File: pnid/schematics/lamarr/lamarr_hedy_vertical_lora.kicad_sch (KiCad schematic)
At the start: 59 parts, among them U1 Rocket_Big

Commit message: various fixes
configure lora use,
fix guidance & navigation pnid,
fix retract threshold
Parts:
- removed ClearFlash: Flash:Clear, symbol PnID-Lib:Label
- removed Logging: Logging, symbol PnID-Lib:Label
- added ClearFlash1: Flash:Clear, symbol PnID-Lib:Label
- added Engine: lora:engine_ecu:LoggingEnabled, symbol PnID-Lib:LED
- added Engine: lora:ecu:FlashStatus, symbol PnID-Lib:LED
- added Fuel: lora:fuel_ecu:LoggingEnabled, symbol PnID-Lib:LED
- added Fuel: lora:fuel_ecu:FlashStatus, symbol PnID-Lib:LED
- added Logging1: Logging, symbol PnID-Lib:Label
- added Ox: lora:ox_ecu:FlashStatus, symbol PnID-Lib:LED
- added Ox: lora:ox_ecu:LoggingEnabled, symbol PnID-Lib:LED
- added RCU: lora:rcu:FlashStatus, symbol PnID-Lib:LED
- added RCU: lora:rcu:LoggingEnabled, symbol PnID-Lib:LED
- Voltages: value RocketVoltages -> RocketVoltagesLora
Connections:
- net at engine.~ (O): now also venturi1.~
- net at ox_venturi.~: now also ox_main_valve.~, ox_venturi_pressure.~; no longer engine.~ (O)
- net at venturi1.~: now also fuel_main_valve.~, fuel_venturi_pressure.~; no longer engine.~ (O)
- new net: engine.~ (O), ox_venturi.~
- new net: OX.~, ox_main_valve.~, ox_quick_connect.~
- new net: Orifice1.~, ox_pressurant_valve.~, pressurantPressureRegulator2.~
- new net: FUEL.~, fuel_main_valve.~, ox_quick_connect1.~
- new net: Orifice2.~, fuel_pressurant_valve.~, pressurantPressureRegulator1.~

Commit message: i mog schlafn
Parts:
- Engine: value lora:ecu:FlashStatus -> lora:engine_ecu:FlashStatus
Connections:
- net at engine.~ (O): now also venturi1.~
- net at ox_venturi.~: now also ox_main_valve.~, ox_venturi_pressure.~; no longer engine.~ (O)
- net at venturi1.~: now also fuel_main_valve.~, fuel_venturi_pressure.~; no longer engine.~ (O)
- new net: engine.~ (O), ox_venturi.~
- new net: OX.~, ox_main_valve.~, ox_quick_connect.~
- new net: Orifice1.~, ox_pressurant_valve.~, pressurantPressureRegulator2.~
- new net: FUEL.~, fuel_main_valve.~, ox_quick_connect1.~
- new net: Orifice2.~, fuel_pressurant_valve.~, pressurantPressureRegulator1.~
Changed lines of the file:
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@@
 			)
 		)
-		(property "Value" "lora:ecu:FlashStatus"
+		(property "Value" "lora:engine_ecu:FlashStatus"
 			(at 13.716 -131.318 90)
 			(effects

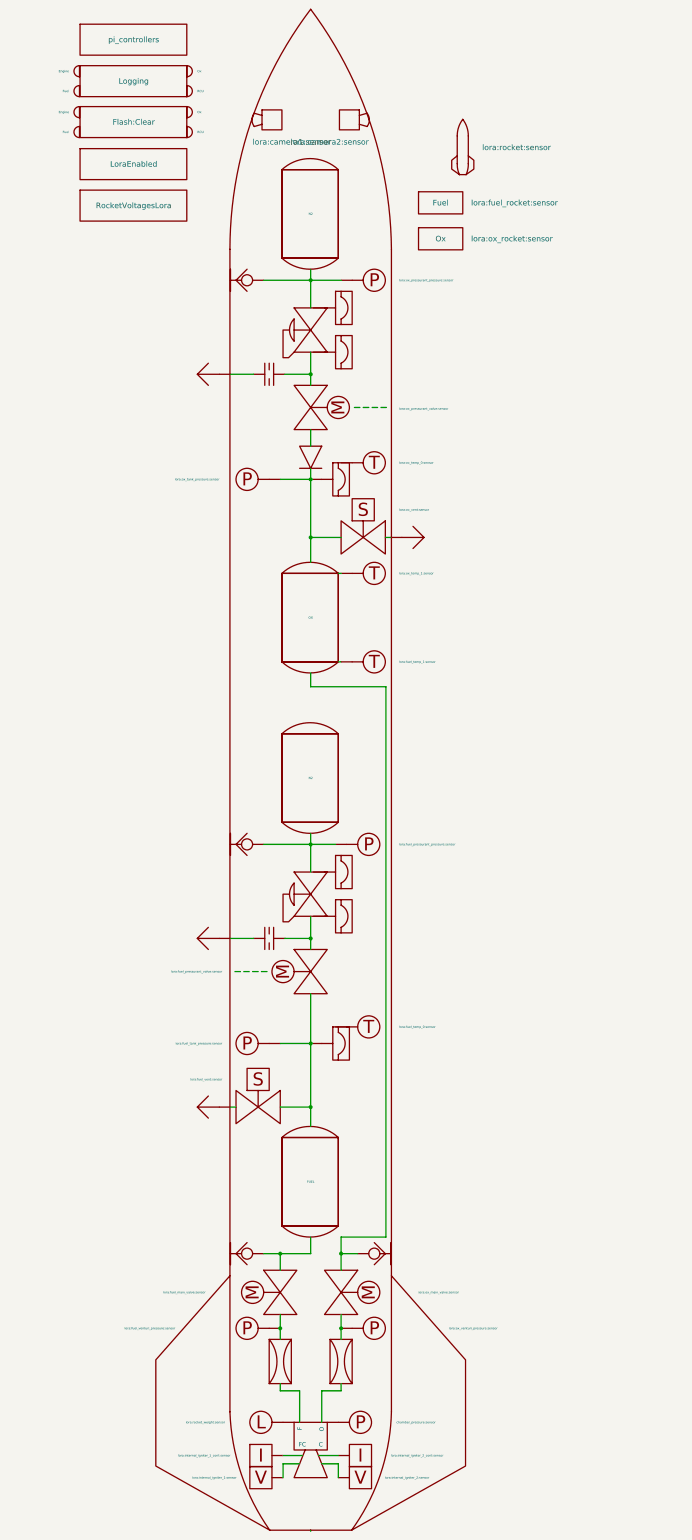
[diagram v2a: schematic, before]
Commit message: more refinements in sensor calibration & ECUI look
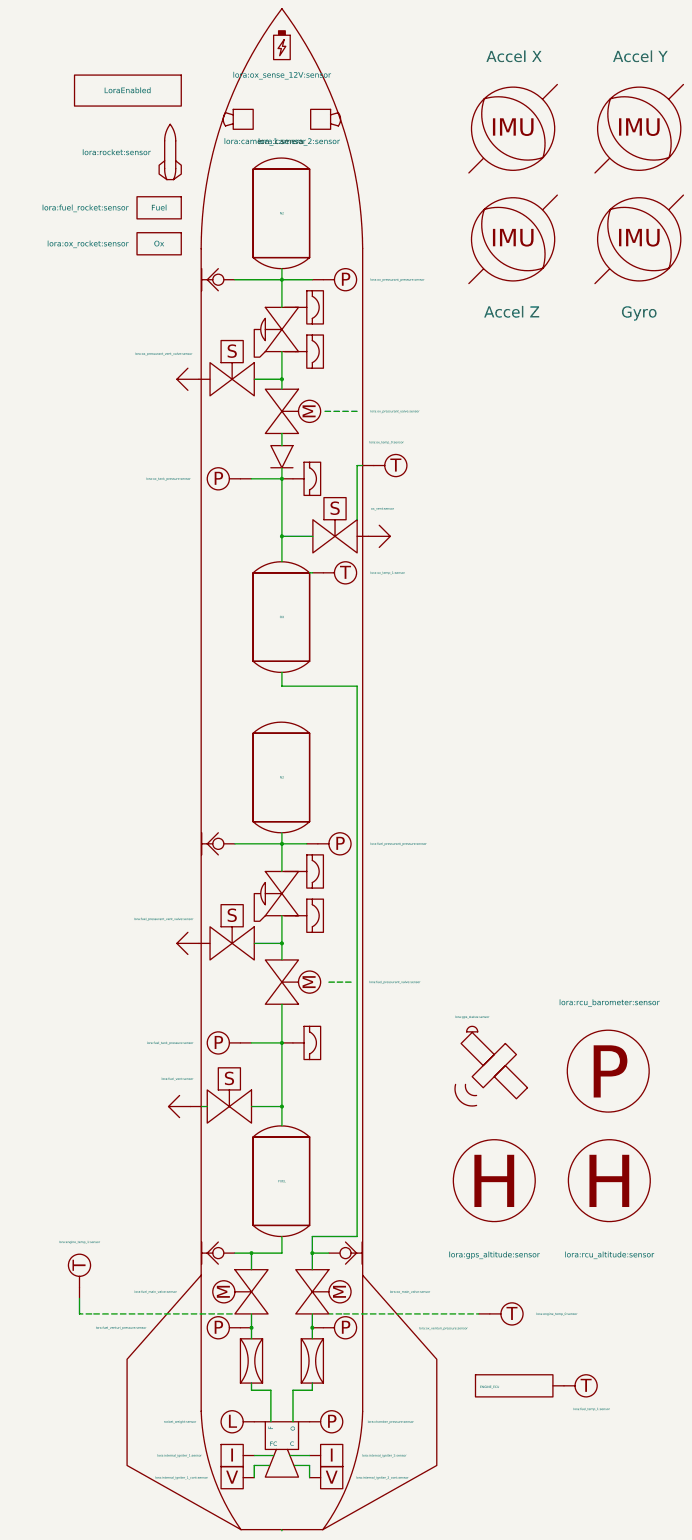
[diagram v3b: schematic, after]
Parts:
- removed ClearFlash1: Flash:Clear, symbol PnID-Lib:Label
- removed Engine: lora:engine_ecu:LoggingEnabled, symbol PnID-Lib:LED
- removed Engine: lora:engine_ecu:FlashStatus, symbol PnID-Lib:LED
- removed Fuel: lora:fuel_ecu:LoggingEnabled, symbol PnID-Lib:LED
- removed Fuel: lora:fuel_ecu:FlashStatus, symbol PnID-Lib:LED
- removed Logging1: Logging, symbol PnID-Lib:Label
- removed Orifice1, Orifice2: Orifice, symbol PnID-Lib:Orifice
- removed Ox: lora:ox_ecu:FlashStatus, symbol PnID-Lib:LED
- removed Ox: lora:ox_ecu:LoggingEnabled, symbol PnID-Lib:LED
- removed PI_Contollers: pi_controllers, symbol PnID-Lib:Label
- removed RCU: lora:rcu:FlashStatus, symbol PnID-Lib:LED
- removed RCU: lora:rcu:LoggingEnabled, symbol PnID-Lib:LED
- removed Voltages: RocketVoltagesLora, symbol PnID-Lib:Label
- removed fuel_manifold_temperature: lora:fuel_temp_0:sensor, symbol PnID-Lib:Sensor_Temperature
- removed ox_manifold_temperature: lora:ox_temp_0:sensor, symbol PnID-Lib:Sensor_Temperature
- added Accel_X: accel_x, symbol PnID-Lib:IMU
- added Accel_Y: accel_y, symbol PnID-Lib:IMU
- added Accel_Z: accel_z, symbol PnID-Lib:IMU
- added Gyro: gyro_x_y_z, symbol PnID-Lib:IMU
- added U2: lora:ox_sense_12V:sensor, symbol PnID-Lib:Battery
- added ecu_flash_status?: lora:gps_status:sensor, symbol PnID-Lib:LED
- added engine_ECU_temperature: lora:fuel_temp_1:sensor, symbol PnID-Lib:Sensor_Temperature
- added engineecu1: ENGINE_ECU, symbol PnID:Label
- added fuel_main_valve_servo_temperature: lora:engine_temp_1:sensor, symbol PnID-Lib:Sensor_Temperature
- added fuel_pressurant_vent_valve: lora:fuel_pressurant_vent_valve:sensor, symbol PnID-Lib:Valve_Solenoid_NO
- added gnss: GNSSLora, symbol PnID-Lib:GNSS
- added gps_altitude: lora:gps_altitude:sensor, symbol PnID-Lib:Sensor_Height
- added ox_pressurant_vent_valve: lora:ox_pressurant_vent_valve:sensor, symbol PnID-Lib:Valve_Solenoid_NO
- added ox_vent_temperature: lora:ox_temp_0:sensor, symbol PnID-Lib:Sensor_Temperature
- added rcu_altitude: lora:rcu_altitude:sensor, symbol PnID-Lib:Sensor_Height
- added rcu_barometer: lora:rcu_barometer:sensor, symbol PnID-Lib:Sensor_Pressure_Big
- C6: value lora:camera2:sensor -> lora:camera_2:sensor
- C7: value lora:camera1:sensor -> lora:camera_1:sensor
- chamber_pressure: value chamber_pressure:sensor -> lora:chamber_pressure:sensor
- igniter1: value lora:internal_igniter_1_cont:sensor -> lora:internal_igniter_1:sensor
- igniter2: value lora:internal_igniter_2_cont:sensor -> lora:internal_igniter_2:sensor
- ox_main_valve_servo_temperature: renamed from ox_tank_bottom_temperature; value lora:fuel_temp_1:sensor -> lora:engine_temp_0:sensor
- ox_vent: value lora:ox_vent:sensor -> ox_vent:sensor
- ox_venturi: value lora:ox_venturi:sensor -> ox_venturi:sensor
- thrust: value lora:rocket_weight:sensor -> rocket_weight:sensor
- venturi1: value lora:venturi:sensor -> venturi:sensor
- voltmeter1: value lora:internal_igniter_1:sensor -> lora:internal_igniter_1_cont:sensor
- voltmeter2: value lora:internal_igniter_2:sensor -> lora:internal_igniter_2_cont:sensor
- renumbered R1 to rocket
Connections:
- net at engine.~ (C): now also venturi1.~
- net at ox_venturi.~: now also ox_main_valve.~, ox_venturi_pressure.~; no longer engine.~ (O)
- net at venturi1.~: now also fuel_main_valve.~, fuel_venturi_pressure.~; no longer engine.~ (O)
- net at ox_pressurant_valve.~, pressurantPressureRegulator2.~: now also ox_pressurant_vent_valve.~
- net at fuel_pressurant_valve.~, pressurantPressureRegulator1.~: now also fuel_pressurant_vent_valve.~
- net at Vent5.~: now also fuel_pressurant_vent_valve.~
- net at Vent4.~: now also ox_pressurant_vent_valve.~
- new net: engine.~ (C), ox_venturi.~
- new net: OX.~, ox_main_valve.~, ox_quick_connect.~
- new net: FUEL.~, fuel_main_valve.~, ox_quick_connect1.~
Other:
- moved on the sheet: FUEL, Fuel, N2, OX, Ox
